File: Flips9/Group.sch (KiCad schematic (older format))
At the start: 6 parts, among them U301 74238, U302 ULN2803/2003, U303 74238, U304 TD62783

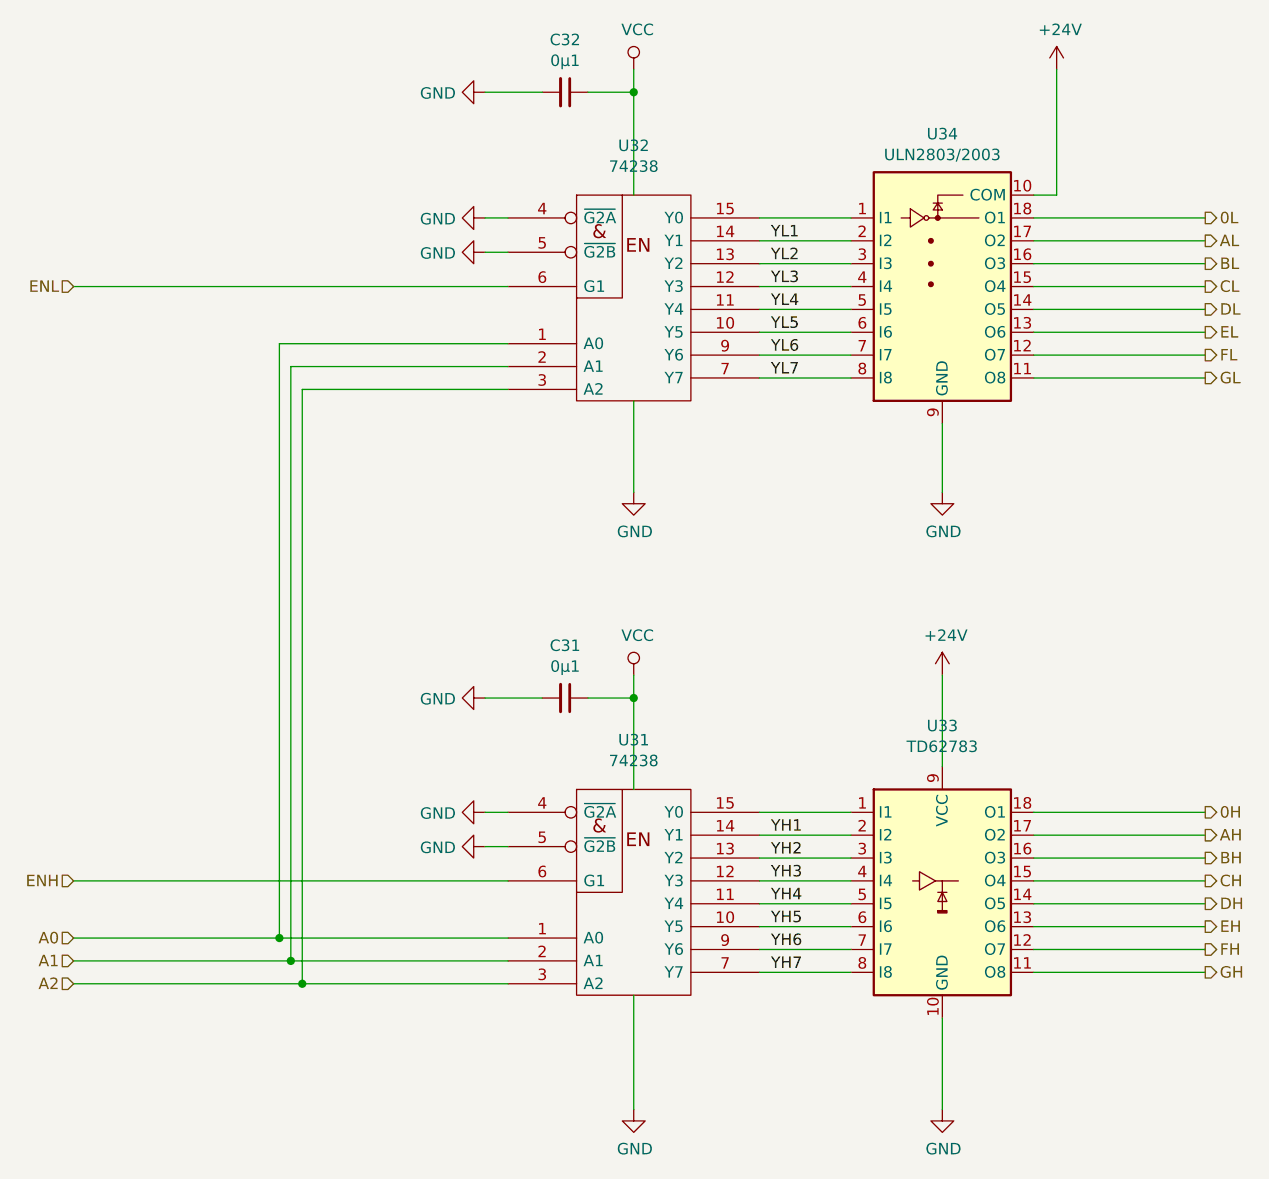
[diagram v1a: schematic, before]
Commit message: Adding capacitors, moving main decoder
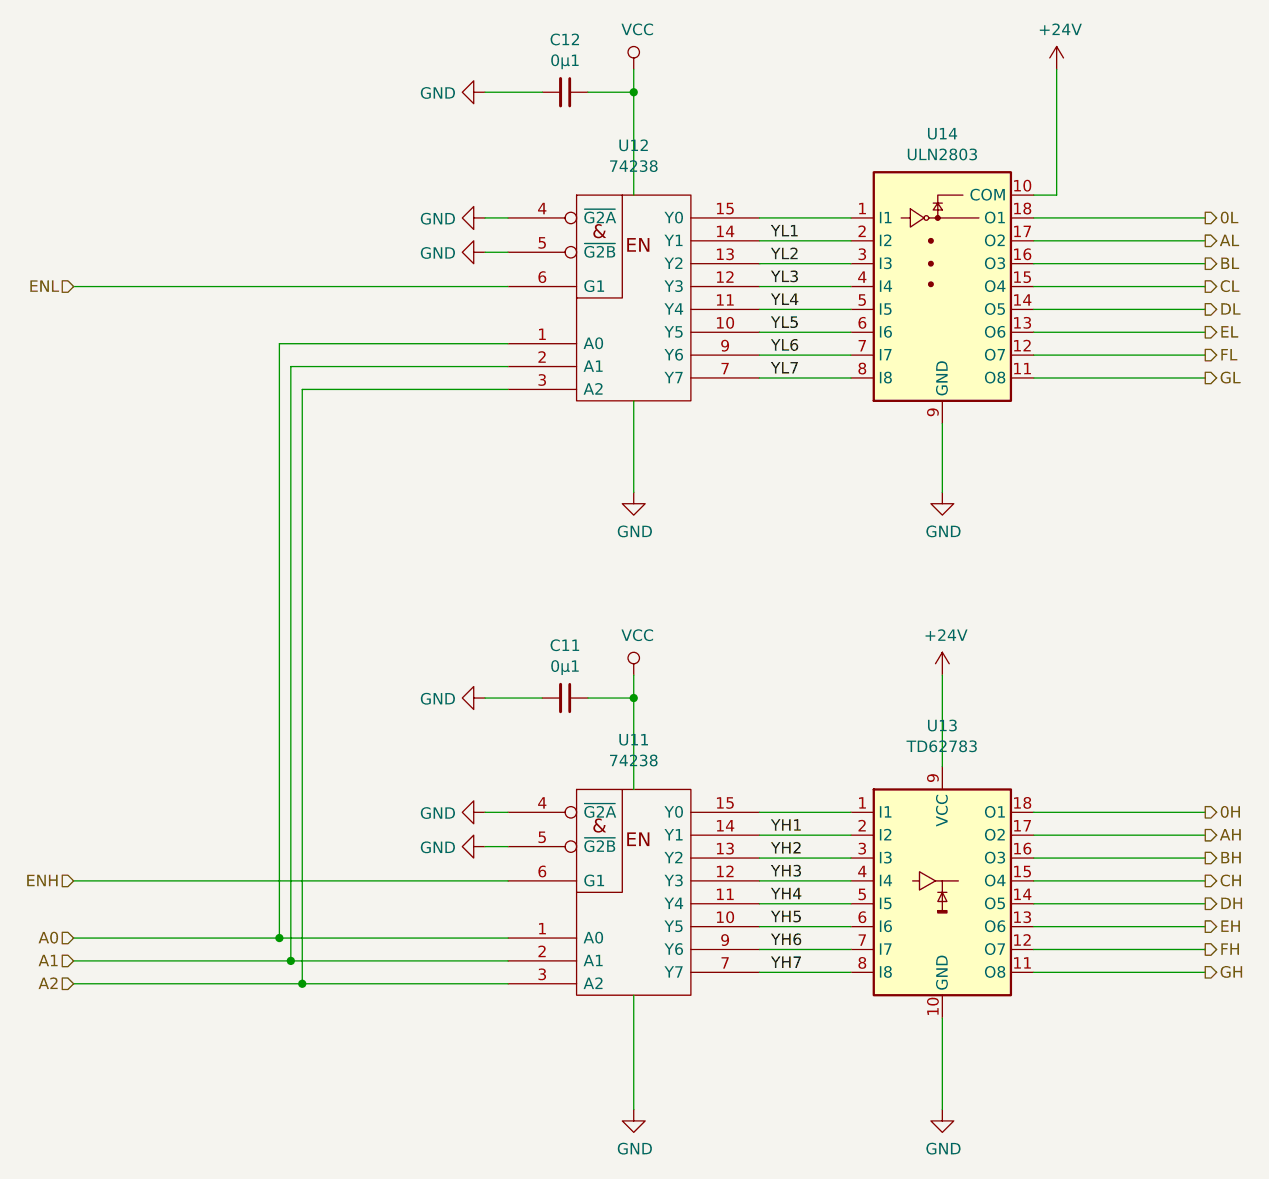
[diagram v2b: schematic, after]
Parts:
- U302: value ULN2803/2003 -> ULN2803
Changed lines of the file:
@@
 $Descr A4 11693 8268
 encoding utf-8
-Sheet 5 6
+Sheet 3 6
 Title ""
 Date ""
@@
 AR Path="/5C4DA960/5C4DAABF/5C4CE34D" Ref="U43"  Part="1"
 AR Path="/5C4DA960/5C8332F1/5C4CE34D" Ref="U43"  Part="1"
-F 0 "U33" H 5900 4978 50  0000 C CNN
+F 0 "U13" H 5900 4978 50  0000 C CNN
 F 1 "TD62783" H 5900 4887 50  0000 C CNN
 F 2 "Housings_DIP:DIP-18_W7.62mm_Socket" H 5900 3750 50  0001 C CNN
@@
 AR Path="/5C4DA960/5C4DAABF/5C4CE354" Ref="U42"  Part="1"
 AR Path="/5C4DA960/5C8332F1/5C4CE354" Ref="U42"  Part="1"
-F 0 "U32" H 4550 2116 50  0000 C CNN
+F 0 "U12" H 4550 2116 50  0000 C CNN
 F 1 "74238" H 4550 2025 50  0000 C CNN
 F 2 "Housings_SOIC:SOIC-16_3.9x9.9mm_Pitch1.27mm" H 4550 1600 50  0001 C CNN
@@
 AR Path="/5C4DA960/5C4DAABF/5C4CE35B" Ref="U41"  Part="1"
 AR Path="/5C4DA960/5C8332F1/5C4CE35B" Ref="U41"  Part="1"
-F 0 "U31" H 4550 4716 50  0000 C CNN
+F 0 "U11" H 4550 4716 50  0000 C CNN
 F 1 "74238" H 4550 4625 50  0000 C CNN
 F 2 "Housings_SOIC:SOIC-16_3.9x9.9mm_Pitch1.27mm" H 4550 4200 50  0001 C CNN
@@
 AR Path="/5C4DA960/5C4DAAA8/5C4D1DBE" Ref="#PWR01006"  Part="1"
 AR Path="/5C4DA960/5C4DAABF/5C4D1DBE" Ref="#PWR01106"  Part="1"
-AR Path="/5C4DA960/5C8332F1/5C4D1DBE" Ref="#PWR?"  Part="1"
-F 0 "#PWR01006" H 5900 2350 50  0001 C CNN
+AR Path="/5C4DA960/5C8332F1/5C4D1DBE" Ref="#PWR0109"  Part="1"
+F 0 "#PWR0806" H 5900 2350 50  0001 C CNN
 F 1 "GND" H 5905 2427 50  0000 C CNN
 F 2 "" H 5900 2600 50  0001 C CNN
@@
 AR Path="/5C4DA960/5C4DAAA8/5C4D1DFA" Ref="#PWR01012"  Part="1"
 AR Path="/5C4DA960/5C4DAABF/5C4D1DFA" Ref="#PWR01112"  Part="1"
-AR Path="/5C4DA960/5C8332F1/5C4D1DFA" Ref="#PWR?"  Part="1"
-F 0 "#PWR01012" H 5900 5050 50  0001 C CNN
+AR Path="/5C4DA960/5C8332F1/5C4D1DFA" Ref="#PWR0110"  Part="1"
+F 0 "#PWR0812" H 5900 5050 50  0001 C CNN
 F 1 "GND" H 5905 5127 50  0000 C CNN
 F 2 "" H 5900 5300 50  0001 C CNN
@@
 AR Path="/5C4DA960/5C4DAAA8/5C4D1E20" Ref="#PWR01011"  Part="1"
 AR Path="/5C4DA960/5C4DAABF/5C4D1E20" Ref="#PWR01111"  Part="1"
-AR Path="/5C4DA960/5C8332F1/5C4D1E20" Ref="#PWR?"  Part="1"
-F 0 "#PWR01011" H 4550 5050 50  0001 C CNN
+AR Path="/5C4DA960/5C8332F1/5C4D1E20" Ref="#PWR0111"  Part="1"
+F 0 "#PWR0811" H 4550 5050 50  0001 C CNN
 F 1 "GND" H 4555 5127 50  0000 C CNN
 F 2 "" H 4550 5300 50  0001 C CNN
@@
 AR Path="/5C4DA960/5C4DAAA8/5C4D1E50" Ref="#PWR01005"  Part="1"
 AR Path="/5C4DA960/5C4DAABF/5C4D1E50" Ref="#PWR01105"  Part="1"
-AR Path="/5C4DA960/5C8332F1/5C4D1E50" Ref="#PWR?"  Part="1"
-F 0 "#PWR01005" H 4550 2350 50  0001 C CNN
+AR Path="/5C4DA960/5C8332F1/5C4D1E50" Ref="#PWR0112"  Part="1"
+F 0 "#PWR0805" H 4550 2350 50  0001 C CNN
 F 1 "GND" H 4555 2427 50  0000 C CNN
 F 2 "" H 4550 2600 50  0001 C CNN
@@
 AR Path="/5C4DA960/5C4DAAA8/5C4D1F03" Ref="#PWR01002"  Part="1"
 AR Path="/5C4DA960/5C4DAABF/5C4D1F03" Ref="#PWR01102"  Part="1"
-AR Path="/5C4DA960/5C8332F1/5C4D1F03" Ref="#PWR?"  Part="1"
-F 0 "#PWR01002" H 6400 600 50  0001 C CNN
+AR Path="/5C4DA960/5C8332F1/5C4D1F03" Ref="#PWR0113"  Part="1"
+F 0 "#PWR0802" H 6400 600 50  0001 C CNN
 F 1 "+24V" H 6415 923 50  0000 C CNN
 F 2 "" H 6400 750 50  0001 C CNN
@@
 AR Path="/5C4DA960/5C4DAAA8/5C4D1F1D" Ref="#PWR01008"  Part="1"
 AR Path="/5C4DA960/5C4DAABF/5C4D1F1D" Ref="#PWR01108"  Part="1"
-AR Path="/5C4DA960/5C8332F1/5C4D1F1D" Ref="#PWR?"  Part="1"
-F 0 "#PWR01008" H 5900 3250 50  0001 C CNN
+AR Path="/5C4DA960/5C8332F1/5C4D1F1D" Ref="#PWR0114"  Part="1"
+F 0 "#PWR0808" H 5900 3250 50  0001 C CNN
 F 1 "+24V" H 5915 3573 50  0000 C CNN
 F 2 "" H 5900 3400 50  0001 C CNN
@@
 AR Path="/5C4DA960/5C4DAAA8/5C4D1FAA" Ref="#PWR01001"  Part="1"
 AR Path="/5C4DA960/5C4DAABF/5C4D1FAA" Ref="#PWR01101"  Part="1"
-AR Path="/5C4DA960/5C8332F1/5C4D1FAA" Ref="#PWR?"  Part="1"
-F 0 "#PWR01001" H 4550 600 50  0001 C CNN
+AR Path="/5C4DA960/5C8332F1/5C4D1FAA" Ref="#PWR0115"  Part="1"
+F 0 "#PWR0801" H 4550 600 50  0001 C CNN
 F 1 "VCC" H 4567 923 50  0000 C CNN
 F 2 "" H 4550 750 50  0001 C CNN
@@
 AR Path="/5C4DA960/5C4DAAA8/5C4D1FD4" Ref="#PWR01007"  Part="1"
 AR Path="/5C4DA960/5C4DAABF/5C4D1FD4" Ref="#PWR01107"  Part="1"
-AR Path="/5C4DA960/5C8332F1/5C4D1FD4" Ref="#PWR?"  Part="1"
-F 0 "#PWR01007" H 4550 3250 50  0001 C CNN
+AR Path="/5C4DA960/5C8332F1/5C4D1FD4" Ref="#PWR0116"  Part="1"
+F 0 "#PWR0807" H 4550 3250 50  0001 C CNN
 F 1 "VCC" H 4567 3573 50  0000 C CNN
 F 2 "" H 4550 3400 50  0001 C CNN
@@
 AR Path="/5C4DA960/5C4DAAA8/5C4DA0A7" Ref="#PWR01010"  Part="1"
 AR Path="/5C4DA960/5C4DAABF/5C4DA0A7" Ref="#PWR01110"  Part="1"
-AR Path="/5C4DA960/5C8332F1/5C4DA0A7" Ref="#PWR?"  Part="1"
-F 0 "#PWR01010" H 3900 3900 50  0001 C CNN
+AR Path="/5C4DA960/5C8332F1/5C4DA0A7" Ref="#PWR0117"  Part="1"
+F 0 "#PWR0810" H 3900 3900 50  0001 C CNN
 F 1 "GND" V 3905 4022 50  0000 R CNN
 F 2 "" H 3900 4150 50  0001 C CNN
@@
 AR Path="/5C4DA960/5C4DAABF/5C4E1AEA" Ref="U44"  Part="1"
 AR Path="/5C4DA960/5C8332F1/5C4E1AEA" Ref="U44"  Part="1"
-F 0 "U34" H 5900 2167 50  0000 C CNN
-F 1 "ULN2803/2003" H 5900 2076 50  0000 C CNN
+F 0 "U14" H 5900 2167 50  0000 C CNN
+F 1 "ULN2803" H 5900 2076 50  0000 C CNN
 F 2 "Housings_DIP:DIP-18_W7.62mm_Socket" H 5950 950 50  0001 L CNN
 F 3 "http://www.ti.com/lit/ds/symlink/uln2803a.pdf" H 6000 1400 50  0001 C CNN
@@
 AR Path="/5C4DA960/5C4DAABF/5C4F67EE" Ref="C41"  Part="1"
 AR Path="/5C4DA960/5C8332F1/5C4F67EE" Ref="C41"  Part="1"
-F 0 "C31" V 4021 3500 50  0000 C CNN
+F 0 "C11" V 4021 3500 50  0000 C CNN
 F 1 "0μ1" V 4112 3500 50  0000 C CNN
 F 2 "Capacitors_SMD:C_0805_HandSoldering" H 4250 3500 50  0001 C CNN
@@
 AR Path="/5C4DA960/5C4DAABF/5C4F6885" Ref="C42"  Part="1"
 AR Path="/5C4DA960/5C8332F1/5C4F6885" Ref="C42"  Part="1"
-F 0 "C32" V 4021 850 50  0000 C CNN
+F 0 "C12" V 4021 850 50  0000 C CNN
 F 1 "0μ1" V 4112 850 50  0000 C CNN
 F 2 "Capacitors_SMD:C_0805_HandSoldering" H 4250 850 50  0001 C CNN
@@
 AR Path="/5C4DA960/5C4DAAA8/5C4F6943" Ref="#PWR01003"  Part="1"
 AR Path="/5C4DA960/5C4DAABF/5C4F6943" Ref="#PWR01103"  Part="1"
-AR Path="/5C4DA960/5C8332F1/5C4F6943" Ref="#PWR?"  Part="1"
-F 0 "#PWR01003" H 3900 600 50  0001 C CNN
+AR Path="/5C4DA960/5C8332F1/5C4F6943" Ref="#PWR0118"  Part="1"
+F 0 "#PWR0803" H 3900 600 50  0001 C CNN
 F 1 "GND" V 3905 722 50  0000 R CNN
 F 2 "" H 3900 850 50  0001 C CNN
@@
 AR Path="/5C4DA960/5C4DAAA8/5C4F6978" Ref="#PWR01009"  Part="1"
 AR Path="/5C4DA960/5C4DAABF/5C4F6978" Ref="#PWR01109"  Part="1"
-AR Path="/5C4DA960/5C8332F1/5C4F6978" Ref="#PWR?"  Part="1"
-F 0 "#PWR01009" H 3900 3250 50  0001 C CNN
+AR Path="/5C4DA960/5C8332F1/5C4F6978" Ref="#PWR0119"  Part="1"
+F 0 "#PWR0809" H 3900 3250 50  0001 C CNN
 F 1 "GND" V 3905 3372 50  0000 R CNN
 F 2 "" H 3900 3500 50  0001 C CNN
@@
 AR Path="/5C4DA960/5C4DAAA8/5C4EB0F4" Ref="#PWR0130"  Part="1"
 AR Path="/5C4DA960/5C4DAABF/5C4EB0F4" Ref="#PWR0133"  Part="1"
-AR Path="/5C4DA960/5C8332F1/5C4EB0F4" Ref="#PWR?"  Part="1"
-F 0 "#PWR0130" H 3900 3750 50  0001 C CNN
+AR Path="/5C4DA960/5C8332F1/5C4EB0F4" Ref="#PWR0120"  Part="1"
+F 0 "#PWR0124" H 3900 3750 50  0001 C CNN
 F 1 "GND" V 3905 3872 50  0000 R CNN
 F 2 "" H 3900 4000 50  0001 C CNN
@@
 AR Path="/5C4DA960/5C4DAAA8/5C4EC62E" Ref="#PWR0131"  Part="1"
 AR Path="/5C4DA960/5C4DAABF/5C4EC62E" Ref="#PWR0134"  Part="1"
-AR Path="/5C4DA960/5C8332F1/5C4EC62E" Ref="#PWR?"  Part="1"
-F 0 "#PWR0131" H 3900 1150 50  0001 C CNN
+AR Path="/5C4DA960/5C8332F1/5C4EC62E" Ref="#PWR0121"  Part="1"
+F 0 "#PWR0125" H 3900 1150 50  0001 C CNN
 F 1 "GND" V 3905 1272 50  0000 R CNN
 F 2 "" H 3900 1400 50  0001 C CNN
@@
 AR Path="/5C4DA960/5C4DAAA8/5C4EC645" Ref="#PWR0132"  Part="1"
 AR Path="/5C4DA960/5C4DAABF/5C4EC645" Ref="#PWR0135"  Part="1"
-AR Path="/5C4DA960/5C8332F1/5C4EC645" Ref="#PWR?"  Part="1"
-F 0 "#PWR0132" H 3900 1300 50  0001 C CNN
+AR Path="/5C4DA960/5C8332F1/5C4EC645" Ref="#PWR0122"  Part="1"
+F 0 "#PWR0126" H 3900 1300 50  0001 C CNN
 F 1 "GND" V 3905 1422 50  0000 R CNN
 F 2 "" H 3900 1550 50  0001 C CNN
